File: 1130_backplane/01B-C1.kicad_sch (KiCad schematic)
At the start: 86 parts

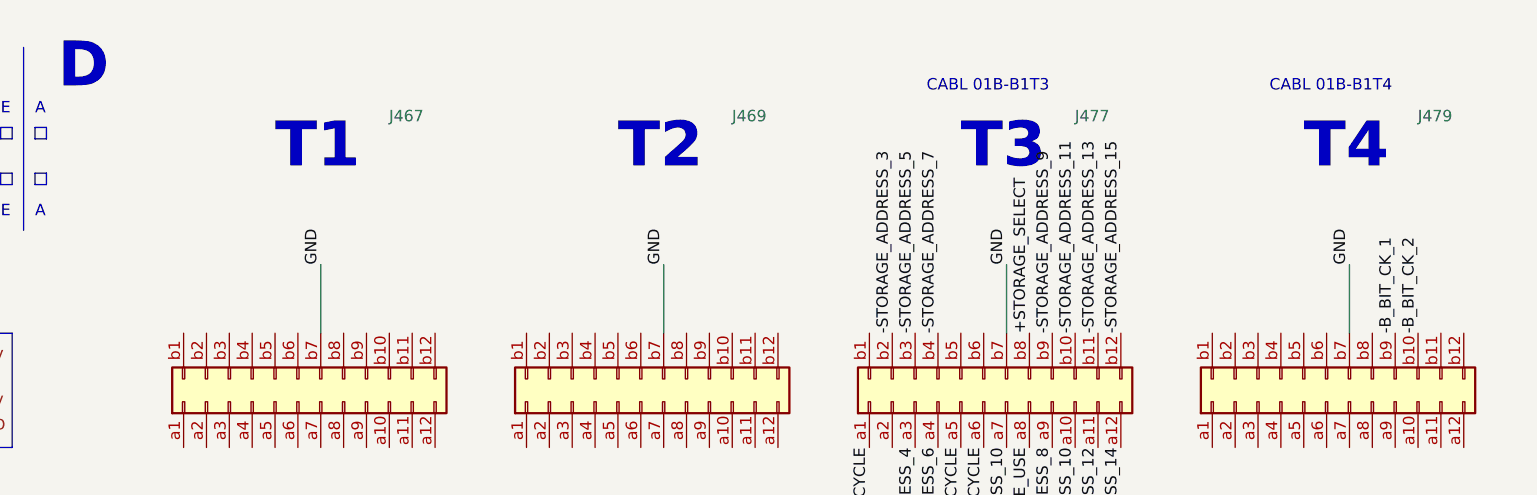
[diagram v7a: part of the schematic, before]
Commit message: Finish page RB101-RB171 and RB201-RB271
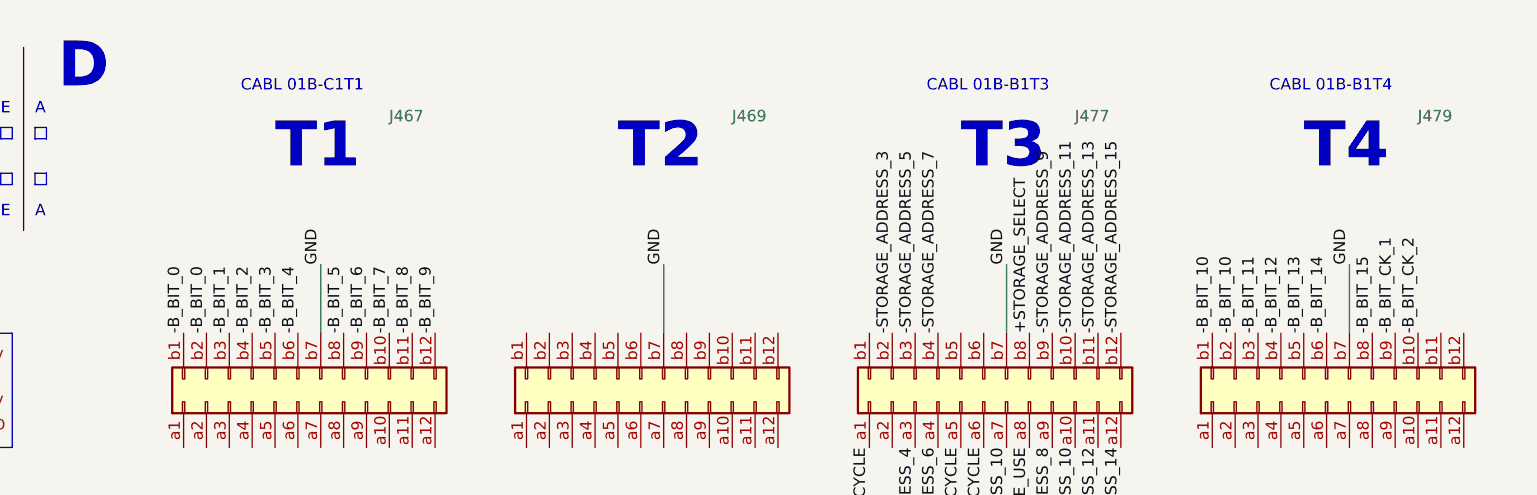
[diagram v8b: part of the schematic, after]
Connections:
- net -B_BIT_0: now reaches J467.b1 (Pin_b1)
- net -B_BIT_0: now also J467.b2 (Pin_b2)
- net -B_BIT_7: now reaches J467.b10 (Pin_b10)
- net -B_BIT_8: now reaches J467.b11 (Pin_b11)
- net -B_BIT_9: now reaches J467.b12 (Pin_b12)
- net -B_BIT_1: now reaches J467.b3 (Pin_b3)
- net -B_BIT_2: now reaches J467.b4 (Pin_b4)
- net -B_BIT_3: now reaches J467.b5 (Pin_b5)
- net -B_BIT_4: now reaches J467.b6 (Pin_b6)
- net -B_BIT_5: now reaches J467.b8 (Pin_b8)
- net -B_BIT_6: now reaches J467.b9 (Pin_b9)
- net -B_BIT_10: now reaches J479.b1 (Pin_b1)
- net -B_BIT_10: now also J479.b2 (Pin_b2)
- net -B_BIT_11: now reaches J479.b3 (Pin_b3)
- net -B_BIT_12: now reaches J479.b4 (Pin_b4)
- net -B_BIT_13: now reaches J479.b5 (Pin_b5)
- net -B_BIT_14: now reaches J479.b6 (Pin_b6)
- net -B_BIT_15: now reaches J479.b8 (Pin_b8)
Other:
- note added: "CABL 01B-C1T1"
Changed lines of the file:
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@@
     (effects (font (size 5 5) (thickness 1) bold) (justify left bottom))
   )
+  (text "CABL 01B-C1T1" (at 355.6 24.13 0)
+    (effects (font (size 1.27 1.27)) (justify left bottom))
+  )
   (label "+3V" (at 624.84 220.98 0)
     (effects (font (size 1.27 1.27)) (justify left bottom))
@@
     (effects (font (size 1.27 1.27)) (justify right bottom))
   )
+  (label "-B_BIT_9" (at 377.19 50.8 90)
+    (effects (font (size 1.27 1.27)) (justify left bottom))
+  )
   (label "+3V" (at 243.84 106.68 0)
     (effects (font (size 1.27 1.27)) (justify left bottom))
@@
     (effects (font (size 1.27 1.27)) (justify right bottom))
   )
+  (label "-B_BIT_8" (at 374.65 50.8 90)
+    (effects (font (size 1.27 1.27)) (justify left bottom))
+  )
   (label "+6V" (at 215.9 127 180)
     (effects (font (size 1.27 1.27)) (justify right bottom))
@@
     (effects (font (size 1.27 1.27)) (justify left bottom))
   )
+  (label "-B_BIT_2" (at 356.87 50.8 90)
+    (effects (font (size 1.27 1.27)) (justify left bottom))
+  )
   (label "+3V" (at 815.34 182.88 0)
     (effects (font (size 1.27 1.27)) (justify left bottom))
@@
     (effects (font (size 1.27 1.27)) (justify right bottom))
   )
+  (label "-B_BIT_6" (at 369.57 50.8 90)
+    (effects (font (size 1.27 1.27)) (justify left bottom))
+  )
   (label "-3V" (at 215.9 114.3 180)
     (effects (font (size 1.27 1.27)) (justify right bottom))
@@
     (effects (font (size 1.27 1.27)) (justify right bottom))
   )
+  (label "-B_BIT_7" (at 372.11 50.8 90)
+    (effects (font (size 1.27 1.27)) (justify left bottom))
+  )
   (label "GND" (at 815.34 309.88 0)
     (effects (font (size 1.27 1.27)) (justify left bottom))
@@
     (effects (font (size 1.27 1.27)) (justify left bottom))
   )
+  (label "-B_BIT_14" (at 476.25 50.8 90)
+    (effects (font (size 1.27 1.27)) (justify left bottom))
+  )
   (label "GND" (at 688.34 233.68 0)
     (effects (font (size 1.27 1.27)) (justify left bottom))
@@
     (effects (font (size 1.27 1.27)) (justify left bottom))
   )
+  (label "-B_BIT_0" (at 351.79 50.8 90)
+    (effects (font (size 1.27 1.27)) (justify left bottom))
+  )
   (label "-3V" (at 152.4 190.5 180)
     (effects (font (size 1.27 1.27)) (justify right bottom))
@@
     (effects (font (size 1.27 1.27)) (justify left bottom))
   )
+  (label "-B_BIT_1" (at 354.33 50.8 90)
+    (effects (font (size 1.27 1.27)) (justify left bottom))
+  )
   (label "+6V" (at 660.4 127 180)
     (effects (font (size 1.27 1.27)) (justify right bottom))
@@
     (effects (font (size 1.27 1.27)) (justify right bottom))
   )
+  (label "-B_BIT_3" (at 359.41 50.8 90)
+    (effects (font (size 1.27 1.27)) (justify left bottom))
+  )
   (label "GND" (at 561.34 157.48 0)
     (effects (font (size 1.27 1.27)) (justify left bottom))
@@
     (effects (font (size 1.27 1.27)) (justify right bottom))
   )
+  (label "-B_BIT_12" (at 471.17 50.8 90)
+    (effects (font (size 1.27 1.27)) (justify left bottom))
+  )
   (label "-3V" (at 723.9 190.5 180)
     (effects (font (size 1.27 1.27)) (justify right bottom))
@@
     (effects (font (size 1.27 1.27)) (justify right bottom))
   )
+  (label "-B_BIT_4" (at 361.95 50.8 90)
+    (effects (font (size 1.27 1.27)) (justify left bottom))
+  )
   (label "+6V" (at 342.9 165.1 180)
     (effects (font (size 1.27 1.27)) (justify right bottom))
@@
     (effects (font (size 1.27 1.27)) (justify right bottom))
   )
+  (label "-B_BIT_13" (at 473.71 50.8 90)
+    (effects (font (size 1.27 1.27)) (justify left bottom))
+  )
   (label "GND" (at 53.34 157.48 0)
     (effects (font (size 1.27 1.27)) (justify left bottom))
@@
     (effects (font (size 1.27 1.27)) (justify right bottom))
   )
+  (label "-B_BIT_15" (at 481.33 50.8 90)
+    (effects (font (size 1.27 1.27)) (justify left bottom))
+  )
   (label "GND" (at 624.84 271.78 0)
     (effects (font (size 1.27 1.27)) (justify left bottom))
@@
     (effects (font (size 1.27 1.27)) (justify left bottom))
   )
+  (label "-B_BIT_11" (at 468.63 50.8 90)
+    (effects (font (size 1.27 1.27)) (justify left bottom))
+  )
   (label "+6V" (at 469.9 317.5 180)
     (effects (font (size 1.27 1.27)) (justify right bottom))
@@
     (effects (font (size 1.27 1.27)) (justify right bottom))
   )
+  (label "-B_BIT_10" (at 463.55 50.8 90)
+    (effects (font (size 1.27 1.27)) (justify left bottom))
+  )
+  (label "-B_BIT_5" (at 367.03 50.8 90)
+    (effects (font (size 1.27 1.27)) (justify left bottom))
+  )
   (label "-STORAGE_ADDRESS_5" (at 430.53 50.8 90)
     (effects (font (size 1.27 1.27)) (justify left bottom))
@@
     (effects (font (size 1.27 1.27)) (justify right bottom))
   )
+  (label "-B_BIT_0" (at 349.25 50.8 90)
+    (effects (font (size 1.27 1.27)) (justify left bottom))
+  )
   (label "GND" (at 243.84 119.38 0)
     (effects (font (size 1.27 1.27)) (justify left bottom))
@@
     (effects (font (size 1.27 1.27)) (justify left bottom))
   )
+  (label "-B_BIT_10" (at 466.09 50.8 90)
+    (effects (font (size 1.27 1.27)) (justify left bottom))
+  )
